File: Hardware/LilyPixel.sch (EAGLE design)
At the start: 15 parts

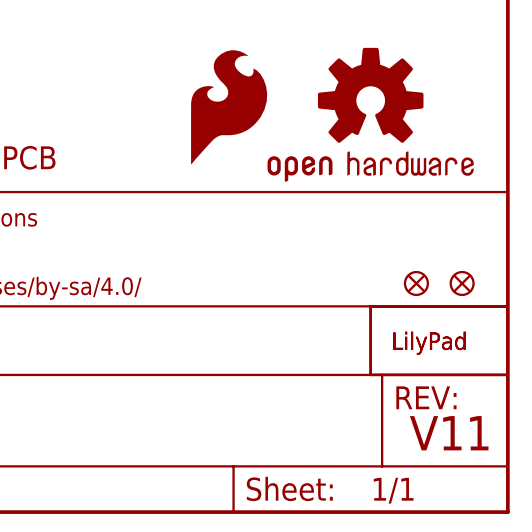
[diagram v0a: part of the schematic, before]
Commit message: added regular fiducials
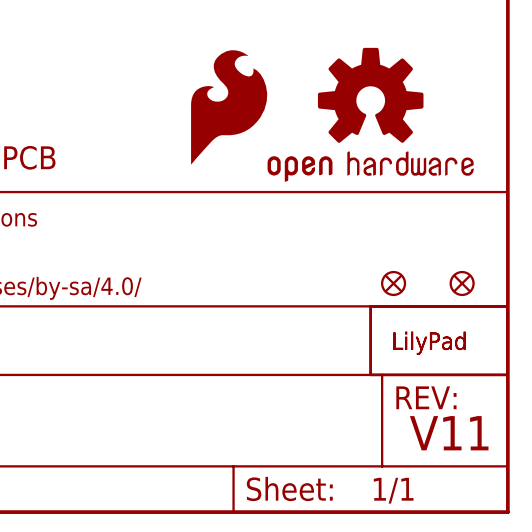
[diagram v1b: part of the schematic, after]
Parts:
- FID1, FID2: value FIDUCIALUFIDUCIAL -> FIDUCIAL1X2; device SparkFun-Aesthetics:FIDUCIALUFIDUCIAL -> SparkFun-Aesthetics:FIDUCIAL1X2
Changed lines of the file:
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@@
 <?xml version="1.0" encoding="utf-8"?>
 <!DOCTYPE eagle SYSTEM "eagle.dtd">
-<eagle version="6.4">
+<eagle version="6.6.0">
 <drawing>
 <settings>
@@
 <part name="LOGO1" library="SparkFun-Aesthetics" deviceset="OSHW-LOGO" device="S"/>
 <part name="LOGO2" library="SparkFun-Aesthetics" deviceset="SFE_LOGO_FLAME" device=".1_INCH"/>
-<part name="FID1" library="SparkFun-Aesthetics" deviceset="FIDUCIAL" device="UFIDUCIAL"/>
-<part name="FID2" library="SparkFun-Aesthetics" deviceset="FIDUCIAL" device="UFIDUCIAL"/>
+<part name="FID1" library="SparkFun-Aesthetics" deviceset="FIDUCIAL" device="1X2"/>
+<part name="FID2" library="SparkFun-Aesthetics" deviceset="FIDUCIAL" device="1X2"/>
 </parts>
 <sheets>
@@
 <instance part="LOGO1" gate="G$1" x="233.68" y="45.72"/>
 <instance part="LOGO2" gate="G$1" x="213.36" y="38.1"/>
-<instance part="FID1" gate="G$1" x="238.76" y="25.4"/>
+<instance part="FID1" gate="G$1" x="236.22" y="25.4"/>
 <instance part="FID2" gate="G$1" x="243.84" y="25.4"/>
 </instances>
